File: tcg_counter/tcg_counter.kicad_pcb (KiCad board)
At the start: 2 copper layers, 63 x 88 mm, 6 parts

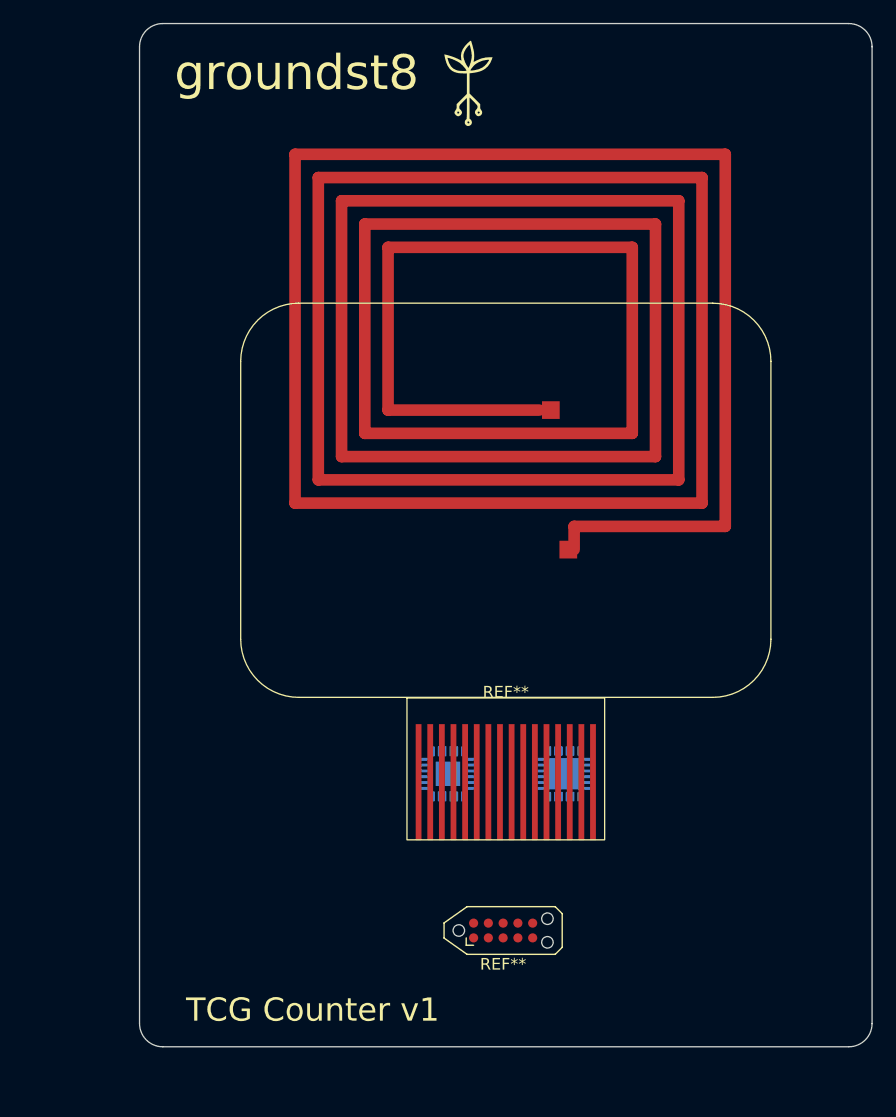
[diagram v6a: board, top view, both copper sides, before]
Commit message: Assigned footprints
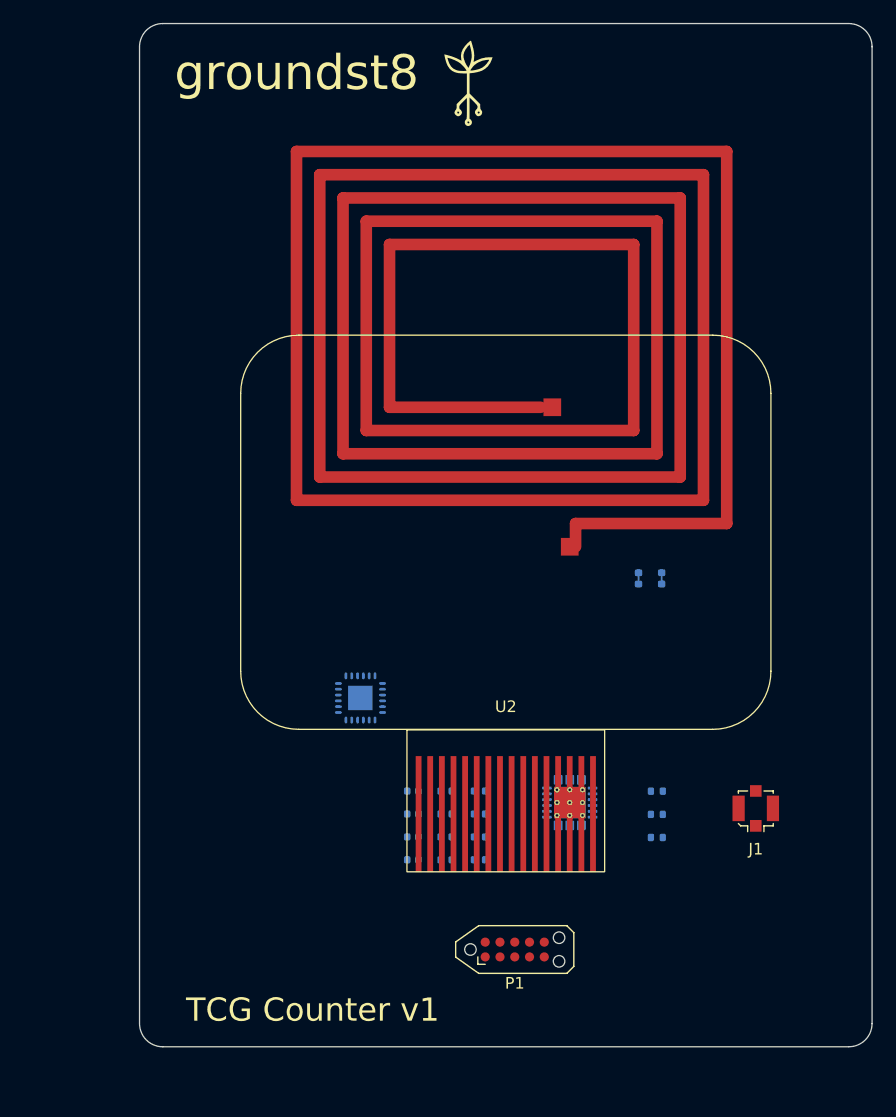
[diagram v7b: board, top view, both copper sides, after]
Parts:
- removed REF**: D0430G02V01, Library:D0430G02V01
- removed REF**: Tag-Connect_TC2050-IDC-NL_2x05_P1.27mm_Vertical_with_bottom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, Connector:Tag-Connect_TC2050-IDC-NL_2x05_P1.27mm_Vertical_with_bottom_clip
- removed REF**: Texas_RTW_WQFN-24-1EP_4x4mm_P0.5mm_EP2.7x2.7mm, Package_DFN_QFN:Texas_RTW_WQFN-24-1EP_4x4mm_P0.5mm_EP2.7x2.7mm
- removed REF**: Texas_RGE0024C_VQFN-24-1EP_4x4mm_P0.5mm_EP2.1x2.1mm, Package_DFN_QFN:Texas_RGE0024C_VQFN-24-1EP_4x4mm_P0.5mm_EP2.1x2.1mm
- added C1: 100nF, Capacitor_SMD:C_0402_1005Metric, B.Cu at (148.2, 108.0)
- added C10: DNP, Capacitor_SMD:C_0402_1005Metric, B.Cu at (142.5, 110.0)
- added C11: 1uF, Capacitor_SMD:C_0402_1005Metric, B.Cu at (142.5, 112.0)
- added C12: 0.1uF, Capacitor_SMD:C_0402_1005Metric, B.Cu at (142.5, 113.9)
- added C2: 2.2µF, Capacitor_SMD:C_0402_1005Metric, B.Cu at (148.2, 110.0)
- added C3: 100nF, Capacitor_SMD:C_0402_1005Metric, B.Cu at (148.2, 112.0)
- added C4: 100nF, Capacitor_SMD:C_0402_1005Metric, B.Cu at (148.2, 113.9)
- added C5: 100nF, Capacitor_SMD:C_0402_1005Metric, B.Cu at (145.4, 108.0)
- added C6: 10nF, Capacitor_SMD:C_0402_1005Metric, B.Cu at (145.4, 110.0)
- added C7: 10nF, Capacitor_SMD:C_0402_1005Metric, B.Cu at (145.4, 112.0)
- added C8: 91pF, Capacitor_SMD:C_0402_1005Metric, B.Cu at (145.4, 113.9)
- added C9: 1µF, Capacitor_SMD:C_0402_1005Metric, B.Cu at (142.5, 108.0)
- added J1: U.FL, Connector_Coaxial:U.FL_Molex_MCRF_73412-0110_Vertical, F.Cu at (172.0, 109.5)
- added P1: TC2050-IDC-430, Connector:Tag-Connect_TC2050-IDC-NL_2x05_P1.27mm_Vertical_with_bottom_clip, F.Cu at (151.3, 121.6)
- added R1: 680, Resistor_SMD:R_0402_1005Metric, B.Cu at (163.5, 108.0)
- added R2: DNP, footprints:R_0402_shorted, B.Cu at (161.9, 89.7)
- added R3: DNP, footprints:R_0402_shorted, B.Cu at (163.9, 89.7)
- added R4: 10k, Resistor_SMD:R_0402_1005Metric, B.Cu at (163.5, 110.0)
- added R5: 10k, Resistor_SMD:R_0402_1005Metric, B.Cu at (163.5, 112.0)
- added U1: TCAL9539RTW, Package_DFN_QFN:Texas_RTW_WQFN-24-1EP_4x4mm_P0.5mm_EP2.7x2.7mm_ThermalVias, B.Cu at (156.0, 109.0)
- added U2: ~, Library:D0430G02V01, F.Cu at (133.0, 102.8)
- added U3: RF430FRL152, footprints:RF430FRL152H, B.Cu at (138.0, 100.0)
- moved L1 0.27 mm to (130.5, 52.0)
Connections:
- L1 pad 1: (no net) -> Net-(J1-In)
- L1 pad 2: (no net) -> Net-(J1-Ext)

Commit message: Work on pcb layout, added no fill zones
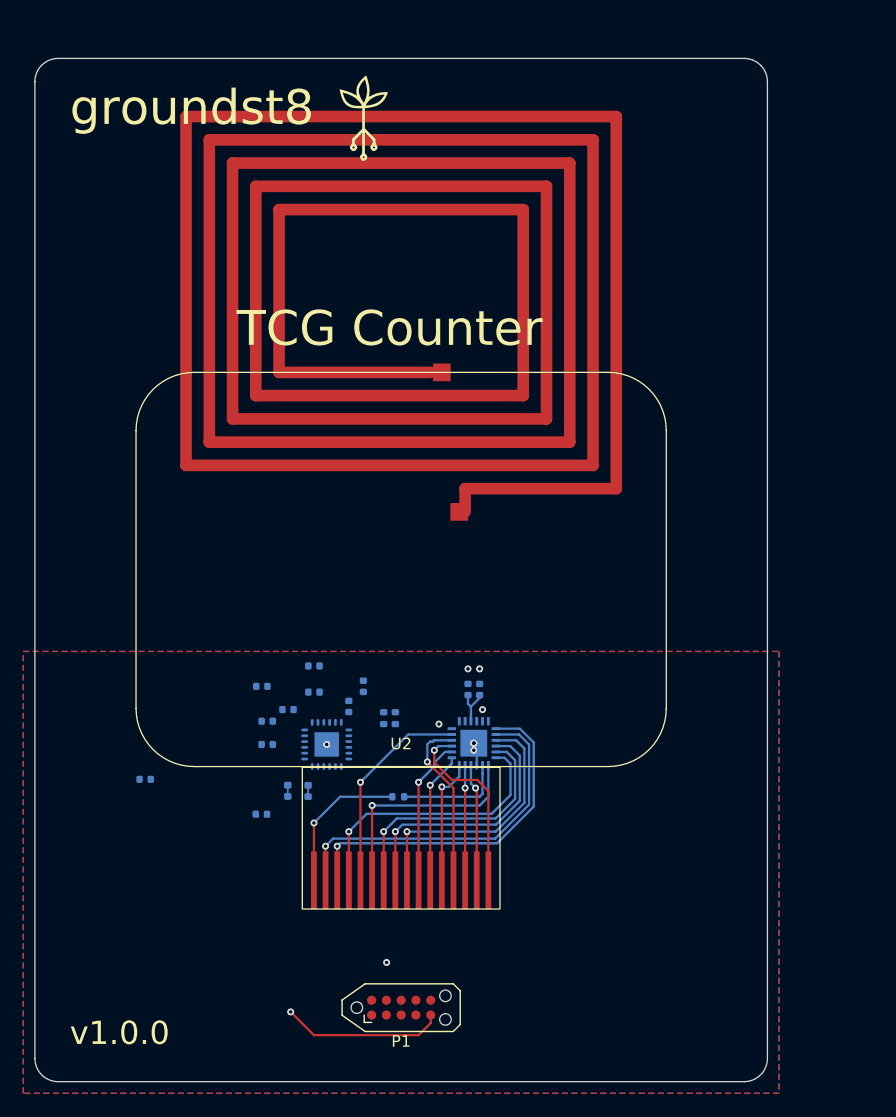
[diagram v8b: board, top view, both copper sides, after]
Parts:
- removed J1: U.FL, Connector_Coaxial:U.FL_Molex_MCRF_73412-0110_Vertical
- R1: value 680 -> 0
- U1: footprint Package_DFN_QFN:Texas_RTW_WQFN-24-1EP_4x4mm_P0.5mm_EP2.7x2.7mm_ThermalVias -> tcal:WQFN24_RTW-J_TEX-L
- moved R3 35.5 mm to (133.5, 108.0)
- moved R2 35.3 mm to (131.8, 108.0)
- moved R4 24.9 mm to (140.0, 101.7), turned to -90 degrees
- moved R5 24.7 mm to (141.0, 101.7), turned to -90 degrees
- moved C9 23.0 mm to (119.5, 107.0)
- moved R1 22.2 mm to (141.2, 108.5)
- moved C3 20.8 mm to (130.0, 102.0)
- moved C4 20.8 mm to (130.0, 104.0)
- moved C1 20.8 mm to (129.5, 99.0)
- moved C8 20.2 mm to (134.0, 97.2), turned to 0 degrees
- moved C2 18.8 mm to (131.8, 101.0)
- moved U2 16.2 mm to (141.5, 89.0)
- moved C6 15.9 mm to (129.5, 110.0)
- moved C12 15.4 mm to (147.2, 99.3), turned to 90 degrees
- moved C7 14.0 mm to (137.0, 100.7), turned to -90 degrees
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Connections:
- U1 pad 25: (no net) -> GND
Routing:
- net Net-(U1-P00): track 0.00 -> 30.5 mm, vias 0 -> 1
- net Net-(U1-P01): track 0.00 -> 30.3 mm, vias 0 -> 1
- net Net-(U1-P05): track 0.00 -> 23.6 mm, vias 0 -> 1
- net Net-(U1-P02): track 0.00 -> 22.7 mm, vias 0 -> 1
- net Net-(U1-P03): track 0.00 -> 22.3 mm, vias 0 -> 1
- net Net-(U1-P04): track 0.00 -> 21.9 mm, vias 0 -> 1
- net Net-(U1-P06): track 0.00 -> 19.5 mm, vias 0 -> 1
- net Net-(U1-P17): track 0.00 -> 18.0 mm, vias 0 -> 1
- net Net-(U1-P15): track 0.00 -> 16.1 mm, vias 0 -> 1
- net Net-(U1-P16): track 0.00 -> 14.9 mm, vias 0 -> 1
- net Net-(U2-COM): track 0.00 -> 14.9 mm, vias 0 -> 1
- net TMS: track 0.00 -> 14.0 mm, vias 0 -> 1
- net Net-(U1-P14): track 0.00 -> 12.6 mm, vias 0 -> 1
- net Net-(U1-P13): track 0.00 -> 11.3 mm, vias 0 -> 1
- net Net-(U1-P12): track 0.00 -> 10.9 mm, vias 0 -> 1
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- added copper zone on B.Cu, net GND
- added copper zone on F.Cu, net GND
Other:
- board text added: "TCG Counter"
- board text added: "v1.0.0"
- board text removed: "TCG Counter v1"
